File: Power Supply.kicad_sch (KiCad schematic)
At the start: 10 parts, among them CN5 Conn_01x08, J1 Conn_01x12

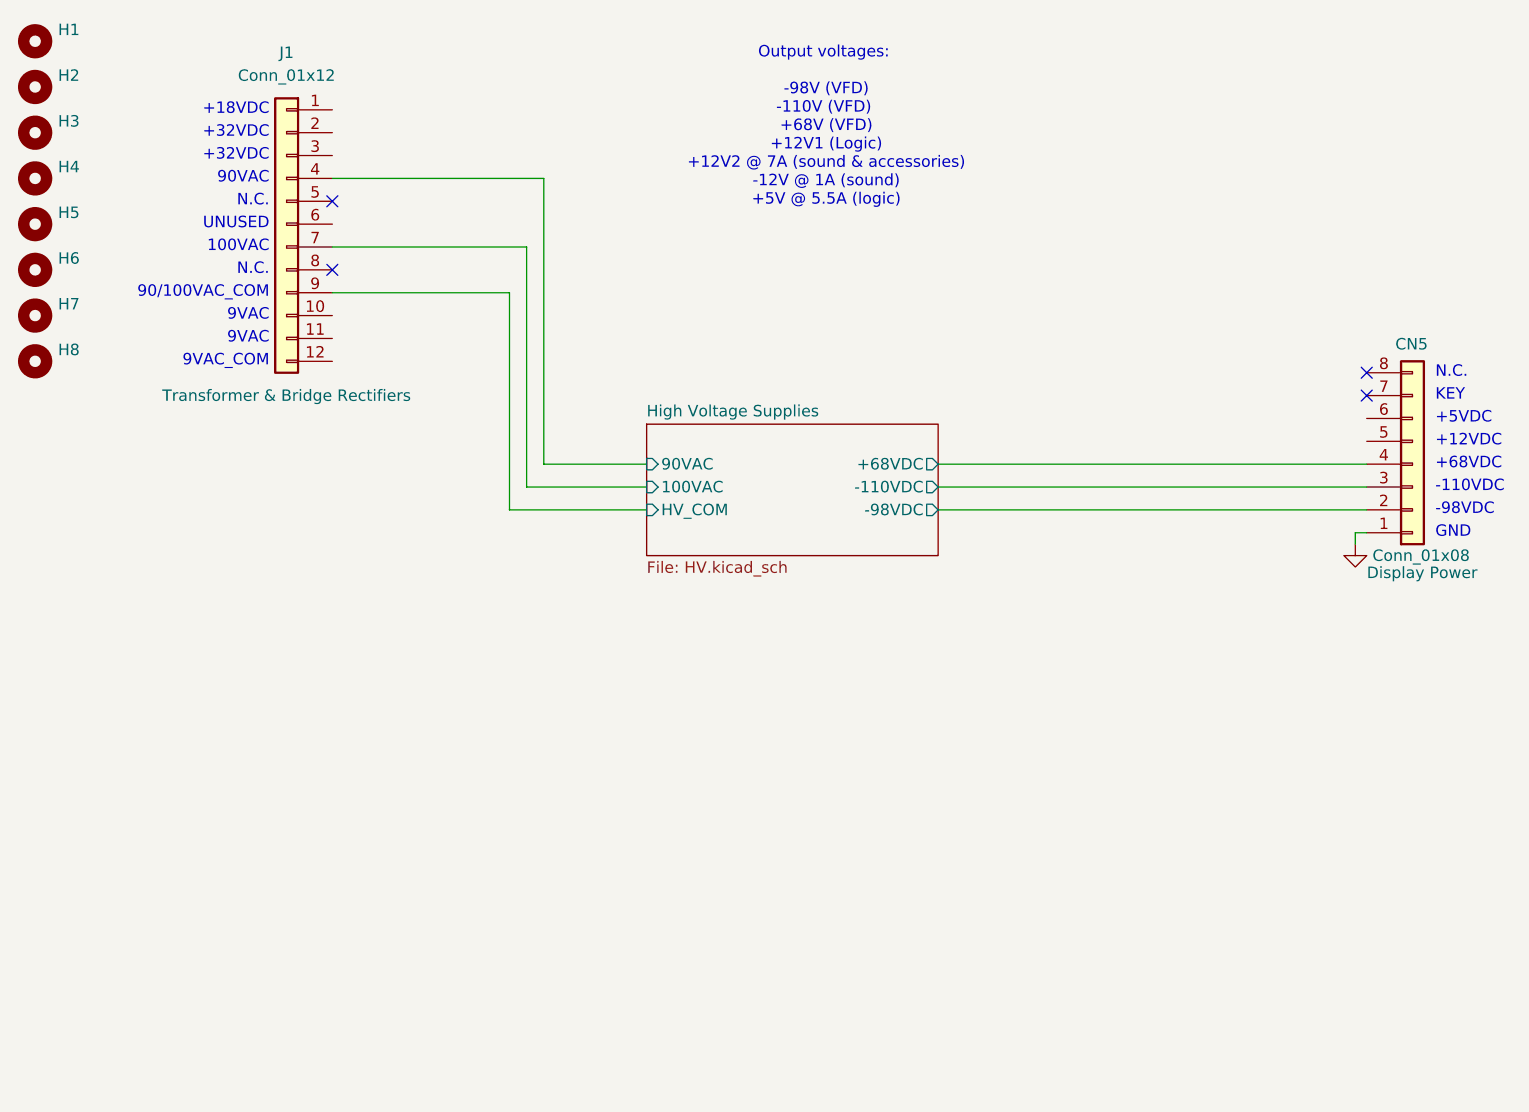
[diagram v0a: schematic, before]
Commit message: Added 5V power supply
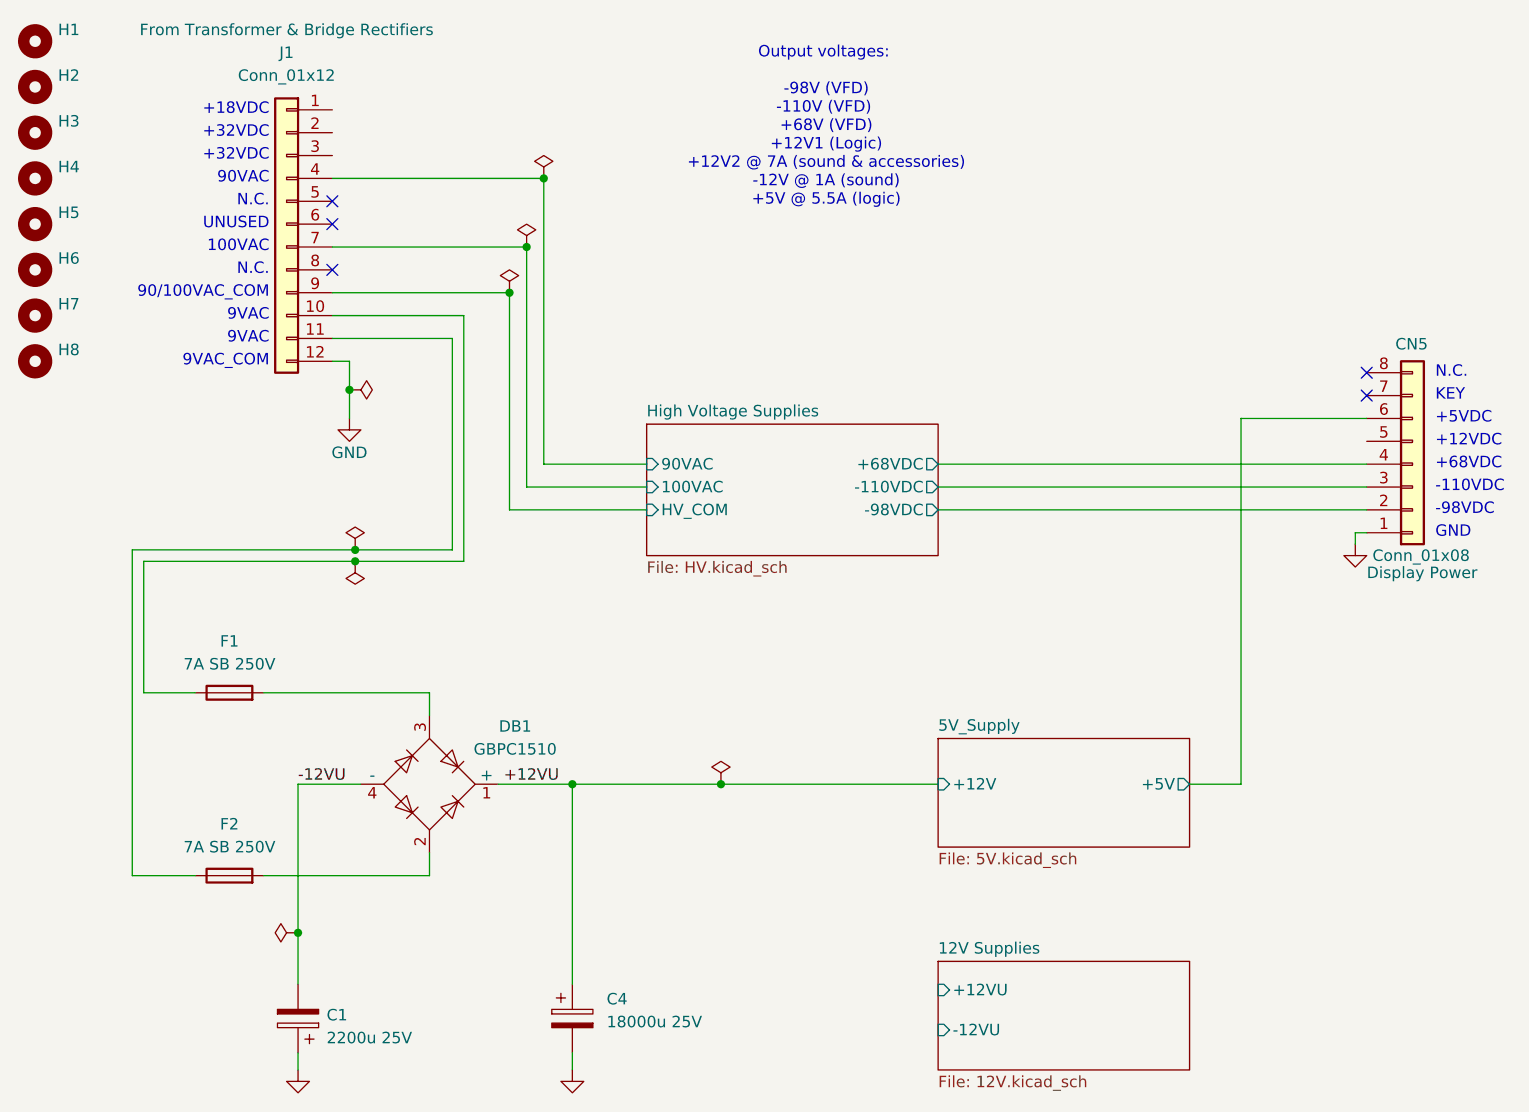
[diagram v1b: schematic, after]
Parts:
- added C1: 2200u 25V, symbol Device:C_Polarized
- added C4: 18000u 25V, symbol Device:C_Polarized
- added DB1: GBPC1510, symbol Diode_Bridge:GBU6A
- added F1, F2: 7A SB 250V, symbol Device:Fuse
- J1: Dest Transformer & Bridge Rectifiers -> From Transformer & Bridge Rectifiers
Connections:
- net GND: now also J1.12 (Pin_12), C1.1, C4.2
- net 5V_Supply/+5V: now reaches CN5.6 (Pin_6)
- net at J1.10 (Pin_10): now also F1.1
- net at J1.11 (Pin_11): now also F2.1
- new net: DB1.2, F2.2
- new net: DB1.3, F1.2
- new net +12VU: C4.1, DB1.1 (+)
- new net -12VU: C1.2, DB1.4 (-)
- no-connect marks 4 -> 5
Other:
- added sheet 12V Supplies (12V.kicad_sch)
- added sheet 5V_Supply (5V.kicad_sch)

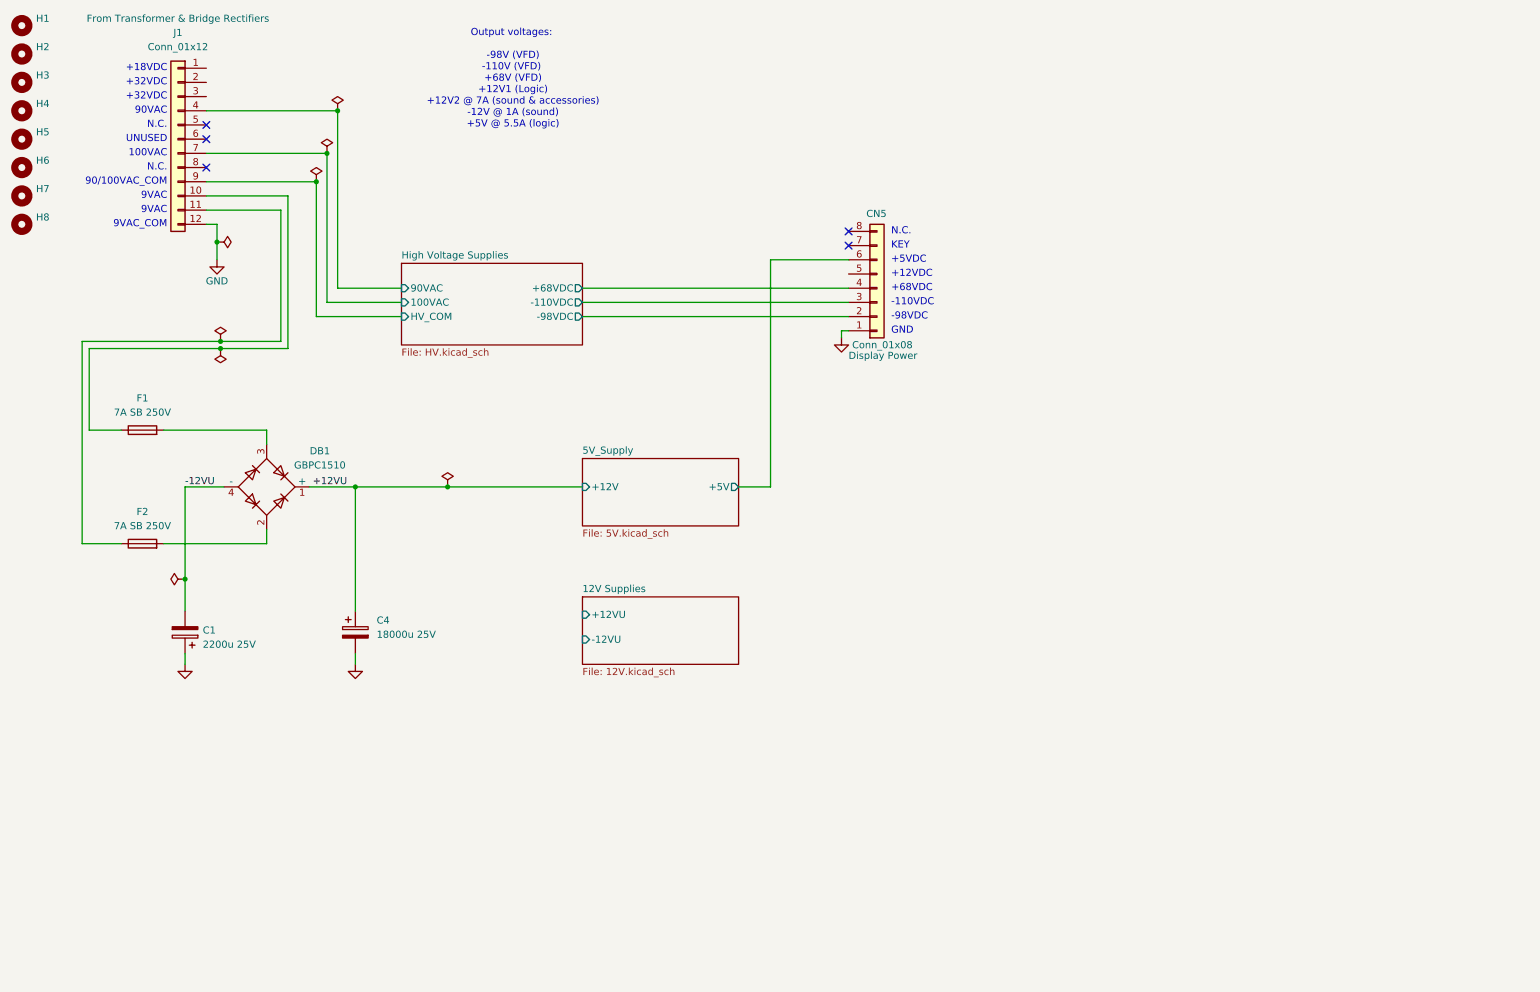
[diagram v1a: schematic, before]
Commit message: Schematic should be finished at this point.  Added more commentary to the README, and ensured all components have footprints assigned.
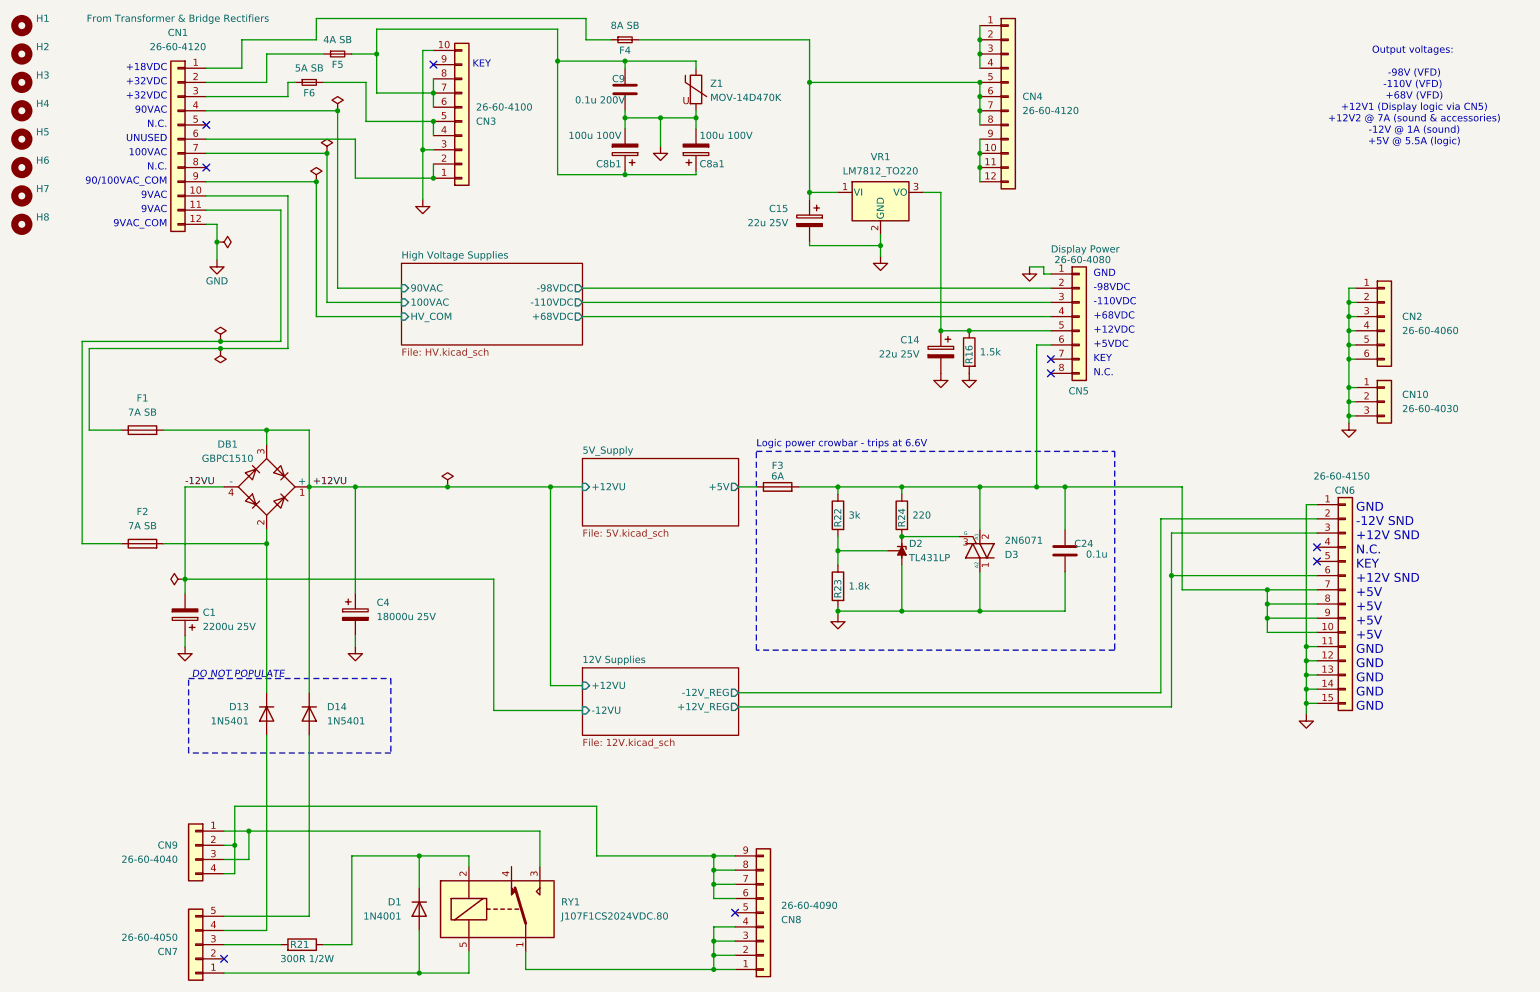
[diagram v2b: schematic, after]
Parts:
- added C14, C15: 22u 25V, Capacitor_THT:CP_Radial_D6.3mm_P2.50mm, symbol Device:C_Polarized
- added C24: 0.1u, Capacitor_SMD:C_1206_3216Metric_Pad1.33x1.80mm_HandSolder, symbol Device:C
- added C8a1, C8b1: 100u 100V, Capacitor_THT:CP_Radial_D10.0mm_P5.00mm, symbol Device:C_Polarized
- added C9: 0.1u 200V, Capacitor_THT:C_Rect_L4.6mm_W3.0mm_P2.50mm_MKS02_FKP02, symbol Device:C
- added CN10: 26-60-4030, Connector_Molex:Molex_KK-396_A-41791-0003_1x03_P3.96mm_Vertical, symbol Connector_Generic:Conn_01x03
- added CN2: 26-60-4060, Connector_Molex:Molex_KK-396_A-41791-0006_1x06_P3.96mm_Vertical, symbol Connector_Generic:Conn_01x06
- added CN3: 26-60-4100, Connector_Molex:Molex_KK-396_A-41791-0010_1x10_P3.96mm_Vertical, symbol Connector_Generic:Conn_01x10
- added CN4: 26-60-4120, Connector_Molex:Molex_KK-396_A-41791-0012_1x12_P3.96mm_Vertical, symbol Connector_Generic:Conn_01x12
- added CN6: 26-60-4150, Connector_Molex:Molex_KK-396_A-41791-0015_1x15_P3.96mm_Vertical, symbol Connector_Generic:Conn_01x15
- added CN7: 26-60-4050, Connector_Molex:Molex_KK-396_A-41791-0005_1x05_P3.96mm_Vertical, symbol Connector_Generic:Conn_01x05
- added CN8: 26-60-4090, Connector_Molex:Molex_KK-396_A-41791-0009_1x09_P3.96mm_Vertical, symbol Connector_Generic:Conn_01x09
- added CN9: 26-60-4040, Connector_Molex:Molex_KK-396_A-41791-0004_1x04_P3.96mm_Vertical, symbol Connector_Generic:Conn_01x04
- added D1: 1N4001, Diode_THT:D_DO-41_SOD81_P10.16mm_Horizontal, symbol Diode:1N4004
- added D13, D14: 1N5401, Diode_THT:D_DO-41_SOD81_P10.16mm_Horizontal, symbol Diode:1N4004
- added D2: TL431LP, Package_TO_SOT_THT:TO-92_Inline, symbol Reference_Voltage:TL431LP
- added D3: 2N6071, Package_TO_SOT_THT:TO-220-3_Vertical, symbol Triac_Thyristor:Generic_Triac_A2A1G
- added F3: 6A, Mounts:BelFuse_0679L, symbol Device:Fuse
- added F4: 8A SB, Mounts:Combo_Blade_Barrel_Fuse, symbol Device:Fuse_Small
- added F5: 4A SB, Mounts:Combo_Blade_Barrel_Fuse, symbol Device:Fuse_Small
- added F6: 5A SB, Mounts:Combo_Blade_Barrel_Fuse, symbol Device:Fuse_Small
- added R16: 1.5k, Resistor_THT:R_Axial_DIN0309_L9.0mm_D3.2mm_P15.24mm_Horizontal, symbol Device:R
- added R21: 300R 1/2W, Resistor_THT:R_Axial_DIN0309_L9.0mm_D3.2mm_P15.24mm_Horizontal, symbol Device:R
- added R22: 3k, Resistor_THT:R_Axial_DIN0309_L9.0mm_D3.2mm_P15.24mm_Horizontal, symbol Device:R
- added R23: 1.8k, Resistor_THT:R_Axial_DIN0309_L9.0mm_D3.2mm_P15.24mm_Horizontal, symbol Device:R
- added R24: 220, Resistor_THT:R_Axial_DIN0309_L9.0mm_D3.2mm_P15.24mm_Horizontal, symbol Device:R
- added RY1: J107F1CS2024VDC.80, Mounts:J107F_Relays, symbol Relay:Relay_SPDT
- added VR1: LM7812_TO220, Package_TO_SOT_THT:TO-220-3_Vertical, symbol Regulator_Linear:LM7812_TO220
- added Z1: MOV-14D470K, Varistor:RV_Disc_D21.5mm_W6.1mm_P7.5mm, symbol Device:Varistor
- C1: footprint (none) -> Capacitor_THT:CP_Radial_D12.5mm_P5.00mm
- C4: footprint (none) -> Capacitor_THT:CP_Radial_D35.0mm_P10.00mm_SnapIn
- CN1: renamed from J1; value Conn_01x12 -> 26-60-4120; footprint (none) -> Connector_Molex:Molex_KK-396_A-41791-0012_1x12_P3.96mm_Vertical
- CN5: value Conn_01x08 -> 26-60-4080; footprint (none) -> Connector_Molex:Molex_KK-396_A-41791-0008_1x08_P3.96mm_Vertical
- DB1: footprint (none) -> Mounts:GBPC_QC
- F1, F2: value 7A SB 250V -> 7A SB; footprint (none) -> Mounts:Combo_Blade_Barrel_Fuse; Connector (none) -> 63994-1 x2
- H1, H3: footprint MountingHole:MountingHole_5.5mm_Pad_Via -> Mounts:MountingHole_5.5mm_Keyhole
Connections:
- net +12VU: now also DB1.3, F1.2, D14.1 (K)
- net 5V_Supply/+5V: now also F3.1; no longer CN5.6 (Pin_6)
- net GND: now also C14.2, C15.2, C24.1, C8a1.2, C8b1.2, C9.2, CN10.1 (Pin_1), CN10.2 (Pin_2), CN10.3 (Pin_3), CN2.1 (Pin_1), CN2.2 (Pin_2), CN2.3 (Pin_3), CN2.4 (Pin_4), CN2.5 (Pin_5), CN2.6 (Pin_6), CN3.10 (Pin_10), CN3.3 (Pin_3), CN6.1 (Pin_1), CN6.11 (Pin_11), CN6.12 (Pin_12), CN6.13 (Pin_13), CN6.14 (Pin_14), CN6.15 (Pin_15), D2.2 (A), D3.1 (A2), R16.2, R23.2, VR1.2 (GND), Z1.2
- net at CN5.5 (Pin_5): now also C14.1, R16.1, VR1.3 (VO)
- net at DB1.2, F2.2: now also D13.1 (K)
- net at CN1.1 (Pin_1): now also F4.1
- net at CN1.2 (Pin_2): now also F5.1
- net at CN1.3 (Pin_3): now also F6.1
- net at CN1.6 (Pin_6): now also CN3.1 (Pin_1), CN3.2 (Pin_2)
- new net: C8a1.1, C8b1.1, C9.1, CN3.6 (Pin_6), CN3.7 (Pin_7), CN3.8 (Pin_8), F5.2, Z1.1
- new net: C15.1, CN4.5 (Pin_5), CN4.6 (Pin_6), CN4.7 (Pin_7), CN4.8 (Pin_8), F4.2, VR1.1 (VI)
- new net: CN8.1 (Pin_1), CN8.2 (Pin_2), CN8.3 (Pin_3), CN8.4 (Pin_4), RY1.1
- new net: D1.1 (K), R21.1, RY1.2
- new net: CN9.1 (Pin_1), CN9.3 (Pin_3), RY1.3
- new net: CN7.1 (Pin_1), D1.2 (A), RY1.5
- new net: C24.2, CN5.6 (Pin_6), CN6.10 (Pin_10), CN6.7 (Pin_7), CN6.8 (Pin_8), CN6.9 (Pin_9), D3.2 (A1), F3.2, R22.1, R24.1
- new net: D2.3 (K), D3.3 (G), R24.2
- new net: D2.1 (REF), R22.2, R23.1
- new net: CN8.6 (Pin_6), CN8.7 (Pin_7), CN8.8 (Pin_8), CN8.9 (Pin_9), CN9.2 (Pin_2), CN9.4 (Pin_4)
- new net: CN7.4 (Pin_4), D13.2 (A)
- new net: CN7.3 (Pin_3), R21.2
- new net: CN3.4 (Pin_4), CN3.5 (Pin_5), F6.2
- new net: CN7.5 (Pin_5), D14.2 (A)
- new net: CN4.1 (Pin_1), CN4.2 (Pin_2), CN4.3 (Pin_3), CN4.4 (Pin_4)
- new net: CN4.10 (Pin_10), CN4.11 (Pin_11), CN4.12 (Pin_12), CN4.9 (Pin_9)
- new net 12V Supplies/+12V_REG: CN6.3 (Pin_3), CN6.6 (Pin_6)
- new net 12V Supplies/-12V_REG: CN6.2 (Pin_2)
- no-connect marks 5 -> 9
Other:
- sheet 12V Supplies ports: added +12V_REG, -12V_REG; removed none
- sheet 5V_Supply ports: added +12VU; removed +12V
- note added: "DO NOT POPULATE"
- note added: "GND -12V SND +12V SND N.C. KEY +12V SND +5V +5V +5V +5V GND GND GND GND GND"
- note added: "Logic power crowbar - trips at 6.6V"
- note added: "Output voltages: -98V (VFD) -110V (VFD) +68V (VFD) +12V1 (Display logic via CN5) +12V2 @ 7A (sound & accessories) -12V @ 1A (sound) +5V @ 5.5A (logic)"
- note removed: "Output voltages: -98V (VFD) -110V (VFD) +68V (VFD) +12V1 (Logic) +12V2 @ 7A (sound & accessories) -12V @ 1A (sound) +5V @ 5.5A (logic)"
- moved on the sheet: C1, C4, CN5
